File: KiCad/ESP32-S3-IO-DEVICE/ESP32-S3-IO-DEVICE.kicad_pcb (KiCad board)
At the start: 2 copper layers, 110 x 100 mm, 62 parts, among them J1 Terminal_04, J2 Terminal_04, J3 Terminal_06, J4 Terminal_02, J5 Terminal_04, J6 Terminal_06, Q1 2SC1815, Q10 2SC1815, Q11 2SC1815, Q12 2SC1815, Q2 2SC1815, Q3 2SC1815, Q4 2SC1815, Q5 2SC1815, Q6 2SC1815, Q7 2SC1815, Q8 2SC1815, Q9 2SC1815, U1 ESP32-S3-DevKitC

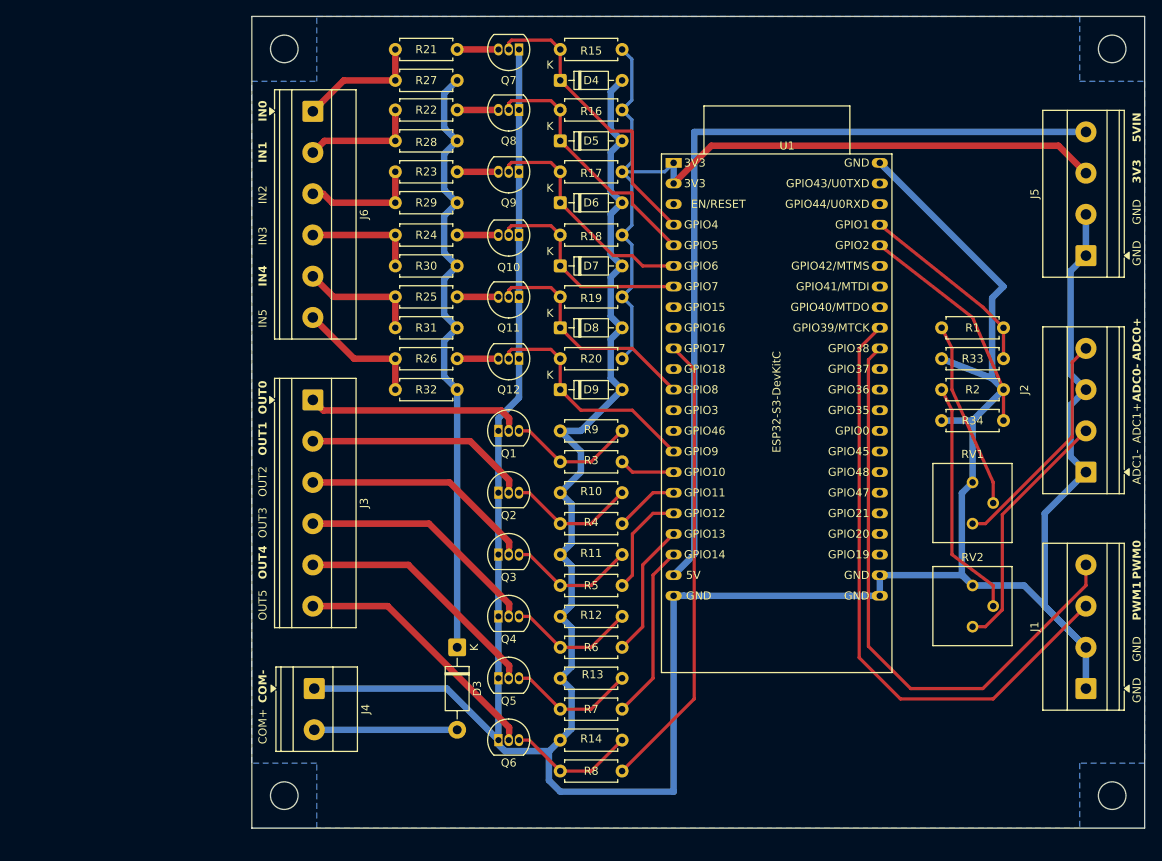
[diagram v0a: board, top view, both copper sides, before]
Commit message: Prepare ESP32IO for public release
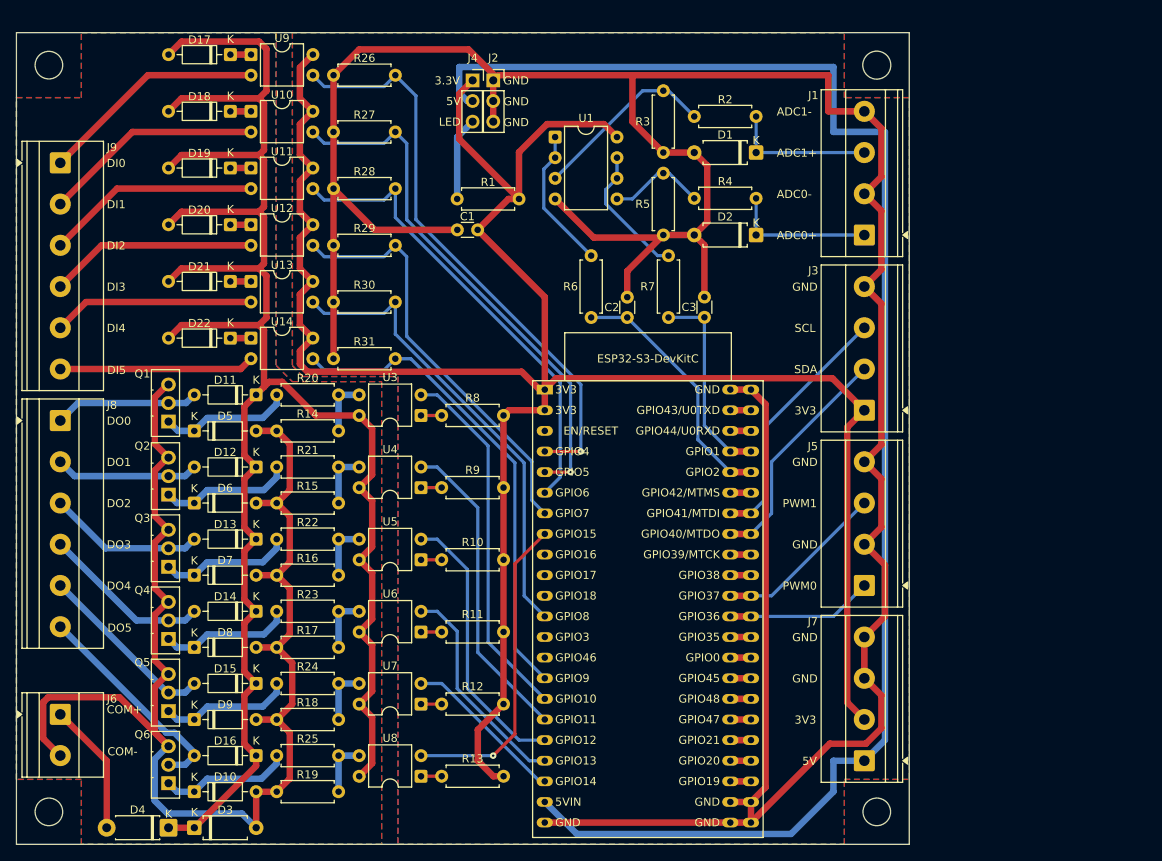
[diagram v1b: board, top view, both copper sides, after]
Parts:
- removed Q10, Q11, Q12, Q7, Q8, Q9: 2SC1815, Package_TO_SOT_THT:TO-92_Inline
- removed R32, R33: 10kΩ, Resistor_THT:R_Axial_DIN0207_L6.3mm_D2.5mm_P7.62mm_Horizontal
- removed R34: 15kΩ, Resistor_THT:R_Axial_DIN0207_L6.3mm_D2.5mm_P7.62mm_Horizontal
- removed RV1, RV2: 10kΩ, Potentiometer_THT:Potentiometer_Bourns_3386P_Vertical
- added C1: 0.1μF, Capacitor_THT:C_Disc_D3.0mm_W1.6mm_P2.50mm, F.Cu at (116.8, 74.3)
- added C2: 0.01μF, Capacitor_THT:C_Disc_D3.0mm_W1.6mm_P2.50mm, F.Cu at (135.3, 85.1)
- added C3: 0.01μF, Capacitor_THT:C_Disc_D3.0mm_W1.6mm_P2.50mm, F.Cu at (144.8, 85.1)
- added D1: P4KE15A, Diode_THT:D_A-405_P7.62mm_Horizontal, F.Cu at (151.1, 64.8)
- added D10: BZX55C12V, Diode_THT:D_DO-35_SOD27_P7.62mm_Horizontal, F.Cu at (81.9, 143.5)
- added D11: 1N4148, Diode_THT:D_DO-35_SOD27_P7.62mm_Horizontal, F.Cu at (89.5, 94.6)
- added D12: 1N4148, Diode_THT:D_DO-35_SOD27_P7.62mm_Horizontal, F.Cu at (89.5, 103.5)
- added D13: 1N4148, Diode_THT:D_DO-35_SOD27_P7.62mm_Horizontal, F.Cu at (89.5, 112.4)
- added D14: 1N4148, Diode_THT:D_DO-35_SOD27_P7.62mm_Horizontal, F.Cu at (89.5, 121.3)
- added D15: 1N4148, Diode_THT:D_DO-35_SOD27_P7.62mm_Horizontal, F.Cu at (89.5, 130.2)
- added D16: 1N4148, Diode_THT:D_DO-35_SOD27_P7.62mm_Horizontal, F.Cu at (89.5, 139.1)
- added D17: E-202, Diode_THT:D_DO-35_SOD27_P7.62mm_Horizontal, F.Cu at (86.4, 52.7)
- added D18: E-202, Diode_THT:D_DO-35_SOD27_P7.62mm_Horizontal, F.Cu at (86.4, 59.7)
- added D19: E-202, Diode_THT:D_DO-35_SOD27_P7.62mm_Horizontal, F.Cu at (86.4, 66.7)
- added D2: P4KE15A, Diode_THT:D_A-405_P7.62mm_Horizontal, F.Cu at (151.1, 74.9)
- added D20: E-202, Diode_THT:D_DO-35_SOD27_P7.62mm_Horizontal, F.Cu at (86.4, 73.7)
- added D21: E-202, Diode_THT:D_DO-35_SOD27_P7.62mm_Horizontal, F.Cu at (86.4, 80.7)
- added D22: E-202, Diode_THT:D_DO-35_SOD27_P7.62mm_Horizontal, F.Cu at (86.4, 87.6)
- added J7: Terminal_04, TerminalBlock_Phoenix:TerminalBlock_Phoenix_MKDS-1,5-4-5.08_1x04_P5.08mm_Horizontal, F.Cu at (164.5, 139.7)
- added J8: Terminal_06, TerminalBlock_Phoenix:TerminalBlock_Phoenix_MKDS-1,5-6-5.08_1x06_P5.08mm_Horizontal, F.Cu at (65.4, 97.8)
- added J9: Terminal_06, TerminalBlock_Phoenix:TerminalBlock_Phoenix_MKDS-1,5-6-5.08_1x06_P5.08mm_Horizontal, F.Cu at (65.4, 66.0)
- added U10: PC817, Package_DIP:DIP-4_W7.62mm, F.Cu at (88.9, 59.7)
- added U11: PC817, Package_DIP:DIP-4_W7.62mm, F.Cu at (88.9, 66.7)
- added U12: PC817, Package_DIP:DIP-4_W7.62mm, F.Cu at (88.9, 73.7)
- added U13: PC817, Package_DIP:DIP-4_W7.62mm, F.Cu at (88.9, 80.7)
- added U14: PC817, Package_DIP:DIP-4_W7.62mm, F.Cu at (88.9, 87.6)
- added U2: ESP32-S3-DevKitC, Espressif:ESP32-S3-DevKitC_3rd_party, F.Cu at (136.5, 119.4)
- added U3: PC817, Package_DIP:DIP-4_W7.62mm, F.Cu at (109.8, 97.2)
- added U4: PC817, Package_DIP:DIP-4_W7.62mm, F.Cu at (109.8, 106.1)
- added U5: PC817, Package_DIP:DIP-4_W7.62mm, F.Cu at (109.8, 114.9)
- added U6: PC817, Package_DIP:DIP-4_W7.62mm, F.Cu at (109.8, 123.8)
- added U7: PC817, Package_DIP:DIP-4_W7.62mm, F.Cu at (109.8, 132.7)
- added U8: PC817, Package_DIP:DIP-4_W7.62mm, F.Cu at (109.8, 141.6)
- added U9: PC817, Package_DIP:DIP-4_W7.62mm, F.Cu at (88.9, 52.7)
- D3: value 1N5819 -> P6KE33A; footprint Diode_THT:D_DO-41_SOD81_P10.16mm_Horizontal -> Diode_THT:D_A-405_P7.62mm_Horizontal
- D4: value BZX55C3V6 -> 1N5819; footprint Diode_THT:D_DO-35_SOD27_P7.62mm_Horizontal -> Diode_THT:D_DO-41_SOD81_P7.62mm_Horizontal
- D5, D6, D7, D8, D9: value BZX55C3V6 -> BZX55C12V
- J2: value Terminal_04 -> Socket_01x03; footprint TerminalBlock_Phoenix:TerminalBlock_Phoenix_MKDS-1,5-4-5.08_1x04_P5.08mm_Horizontal -> Connector_PinSocket_2.54mm:PinSocket_1x03_P2.54mm_Vertical
- J3: value Terminal_06 -> Terminal_04; footprint TerminalBlock_Phoenix:TerminalBlock_Phoenix_MKDS-1,5-6-5.08_1x06_P5.08mm_Horizontal -> TerminalBlock_Phoenix:TerminalBlock_Phoenix_MKDS-1,5-4-5.08_1x04_P5.08mm_Horizontal
- J4: value Terminal_02 -> Socket_01x03; footprint TerminalBlock_Phoenix:TerminalBlock_Phoenix_MKDS-1,5-2-5.08_1x02_P5.08mm_Horizontal -> Connector_PinSocket_2.54mm:PinSocket_1x03_P2.54mm_Vertical
- J6: value Terminal_06 -> Terminal_02; footprint TerminalBlock_Phoenix:TerminalBlock_Phoenix_MKDS-1,5-6-5.08_1x06_P5.08mm_Horizontal -> TerminalBlock_Phoenix:TerminalBlock_Phoenix_MKDS-1,5-2-5.08_1x02_P5.08mm_Horizontal
- Q1, Q2, Q3, Q4, Q5, Q6: value 2SC1815 -> 2SK4017; footprint Package_TO_SOT_THT:TO-92_Inline -> Package_TO_SOT_THT:TO-126-3_Vertical
- R1: value 15kΩ -> 2.2kΩ
- R10, R11, R12, R13, R9: value 100kΩ -> 330Ω
- R14: value 100kΩ -> 10kΩ
- R2: value 10kΩ -> 22kΩ
- R20: value 10kΩ -> 100Ω
- R21, R22, R23, R24, R25: value 47kΩ -> 100Ω
- R27, R28, R29, R30, R31: value 10kΩ -> 47kΩ
- R3, R5: value 680Ω -> 10kΩ
- R4: value 680Ω -> 22kΩ
- R6, R7: value 680Ω -> 100Ω
- R8: value 680Ω -> 330Ω
- U1: value ESP32-S3-DevKitC -> NJU7043D; footprint Espressif:ESP32-S3-DevKitC-1 -> Package_DIP:DIP-8_W7.62mm
- moved D4 104.0 mm to (78.7, 148.0), turned to 180 degrees
- moved J2 87.5 mm to (118.7, 55.9), turned to 0 degrees
- moved J6 80.5 mm to (65.4, 134.0)
- moved J4 77.4 mm to (116.2, 55.9), turned to 0 degrees
- moved R19 70.3 mm to (99.7, 143.5)
- moved R18 69.2 mm to (99.7, 134.6)
- moved R17 68.2 mm to (99.7, 125.7)
- moved J3 68.0 mm to (164.5, 96.5), turned to 90 degrees
- moved R16 67.1 mm to (99.7, 116.8)
- moved R15 65.9 mm to (99.7, 108.0)
- moved J1 62.2 mm to (164.5, 74.9)
- moved R1 61.8 mm to (114.3, 70.5)
- moved D9 60.7 mm to (81.9, 134.6)
- moved D8 59.9 mm to (81.9, 125.7)
- moved D7 59.0 mm to (81.9, 116.8)
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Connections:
- D3 pad 2: Net-(D3-A) -> COM-
- D4 pad 1: Net-(D4-K) -> COM+
- D4 pad 2: GND -> Net-(D4-A)
- D5 pad 2: GND -> COM-
- D6 pad 2: GND -> COM-
- D7 pad 2: GND -> COM-
- D8 pad 2: GND -> COM-
- D9 pad 2: GND -> COM-
- J1 pad 1: GND -> Net-(D2-K)
- J1 pad 3: Net-(J1-Pin_3) -> Net-(D1-K)
- J1 pad 4: Net-(J1-Pin_4) -> GND
- J2 pad 2: Net-(J2-Pin_2) -> GND
- J3 pad 1: Net-(J3-Pin_1) -> 3V3
- J3 pad 4: Net-(J3-Pin_4) -> GND
- J4 pad 1: GND -> 3V3
- J4 pad 2: Net-(D3-A) -> 5V
- J5 pad 1: GND -> Net-(J5-Pin_1)
- J5 pad 3: 3V3 -> Net-(J5-Pin_3)
- J5 pad 4: 5V -> GND
- J6 pad 1: Net-(J6-Pin_1) -> Net-(D4-A)
- J6 pad 2: Net-(J6-Pin_2) -> COM-
- Q1 pad 1: GND -> Net-(D5-K)
- Q1 pad 2: Net-(J3-Pin_1) -> Net-(D11-A)
- Q1 pad 3: Net-(Q1-B) -> COM-
- Q2 pad 1: GND -> Net-(D6-K)
- Q2 pad 2: Net-(J3-Pin_2) -> Net-(D12-A)
- Q2 pad 3: Net-(Q2-B) -> COM-
- Q3 pad 1: GND -> Net-(D7-K)
- Q3 pad 2: Net-(J3-Pin_3) -> Net-(D13-A)
- Q3 pad 3: Net-(Q3-B) -> COM-
- Q4 pad 1: GND -> Net-(D8-K)
- Q4 pad 2: Net-(J3-Pin_4) -> Net-(D14-A)
- Q4 pad 3: Net-(Q4-B) -> COM-
- Q5 pad 1: GND -> Net-(D9-K)
- Q5 pad 2: Net-(J3-Pin_5) -> Net-(D15-A)
- Q5 pad 3: Net-(Q5-B) -> COM-
- Q6 pad 1: GND -> Net-(D10-K)
- Q6 pad 2: Net-(J3-Pin_6) -> Net-(D16-A)
- Q6 pad 3: Net-(Q6-B) -> COM-
- R1 pad 1: Net-(R1-Pad1) -> Net-(J4-Pin_3)
- R1 pad 2: Net-(U1-GPIO1/ADC1_CH0) -> 3V3
- R10 pad 1: Net-(Q2-B) -> 3V3
- R10 pad 2: GND -> Net-(R10-Pad2)
- R11 pad 1: Net-(Q3-B) -> 3V3
- R11 pad 2: GND -> Net-(R11-Pad2)
- R12 pad 1: Net-(Q4-B) -> 3V3
- R12 pad 2: GND -> Net-(R12-Pad2)
- R13 pad 1: Net-(Q5-B) -> 3V3
- R13 pad 2: GND -> Net-(R13-Pad2)
- R14 pad 1: Net-(Q6-B) -> Net-(R14-Pad1)
- R14 pad 2: GND -> COM-
- R15 pad 1: 3V3 -> Net-(R15-Pad1)
- R15 pad 2: Net-(D4-K) -> COM-
- R16 pad 1: 3V3 -> Net-(R16-Pad1)
- R16 pad 2: Net-(D5-K) -> COM-
- R17 pad 1: 3V3 -> Net-(R17-Pad1)
- R17 pad 2: Net-(D6-K) -> COM-
- R18 pad 1: 3V3 -> Net-(R18-Pad1)
- R18 pad 2: Net-(D7-K) -> COM-
- R19 pad 1: 3V3 -> Net-(R19-Pad1)
- R19 pad 2: Net-(D8-K) -> COM-
- R2 pad 1: Net-(R2-Pad1) -> Net-(D1-K)
- R2 pad 2: Net-(U1-GPIO2/ADC1_CH1) -> Net-(U1A-+)
- R20 pad 1: 3V3 -> Net-(R14-Pad1)
- R20 pad 2: Net-(D9-K) -> Net-(D5-K)
- R21 pad 1: Net-(Q7-B) -> Net-(R15-Pad1)
- R21 pad 2: Net-(J6-Pin_1) -> Net-(D6-K)
- R22 pad 1: Net-(Q8-B) -> Net-(R16-Pad1)
- R22 pad 2: Net-(J6-Pin_2) -> Net-(D7-K)
- R23 pad 1: Net-(Q9-B) -> Net-(R17-Pad1)
- R23 pad 2: Net-(J6-Pin_3) -> Net-(D8-K)
- R24 pad 1: Net-(Q10-B) -> Net-(R18-Pad1)
- R24 pad 2: Net-(J6-Pin_4) -> Net-(D9-K)
- R25 pad 1: Net-(Q11-B) -> Net-(R19-Pad1)
- R25 pad 2: Net-(J6-Pin_5) -> Net-(D10-K)
- R26 pad 2: Net-(J6-Pin_6) -> GND
- R27 pad 1: COM+ -> Net-(U2-GPIO5/ADC1_CH4)
- R27 pad 2: Net-(J6-Pin_1) -> GND
- R28 pad 1: COM+ -> Net-(U2-GPIO6/ADC1_CH5)
- R28 pad 2: Net-(J6-Pin_2) -> GND
- R29 pad 1: COM+ -> Net-(U2-GPIO7/ADC1_CH6)
- R29 pad 2: Net-(J6-Pin_3) -> GND
- R3 pad 1: Net-(U1-GPIO10/ADC1_CH9) -> Net-(U1A-+)
- R3 pad 2: Net-(Q1-B) -> GND
- R30 pad 1: COM+ -> Net-(U2-GPIO8/ADC1_CH7)
- R30 pad 2: Net-(J6-Pin_4) -> GND
- R31 pad 1: COM+ -> Net-(U2-GPIO9/ADC1_CH8)
- R31 pad 2: Net-(J6-Pin_5) -> GND
- R4 pad 1: Net-(U1-GPIO11/ADC2_CH0) -> Net-(D2-K)
- R4 pad 2: Net-(Q2-B) -> Net-(U1B-+)
- R5 pad 1: Net-(U1-GPIO12/ADC2_CH1) -> Net-(U1B-+)
- R5 pad 2: Net-(Q3-B) -> GND
- R6 pad 1: Net-(U1-GPIO13/ADC2_CH2) -> Net-(U1A--)
- R6 pad 2: Net-(Q4-B) -> Net-(U2-GPIO2/ADC1_CH1)
- R7 pad 1: Net-(U1-GPIO14/ADC2_CH3) -> Net-(U1B--)
- R7 pad 2: Net-(Q5-B) -> Net-(U2-GPIO1/ADC1_CH0)
- R8 pad 1: Net-(U1-GPIO17/ADC2_CH6) -> 3V3
- R8 pad 2: Net-(Q6-B) -> Net-(R8-Pad2)
- R9 pad 1: Net-(Q1-B) -> 3V3
- R9 pad 2: GND -> Net-(R9-Pad2)
- U1 pad 1: 3V3 -> Net-(U1A--)
- U1 pad 2: 3V3 -> Net-(U1A--)
- U1 pad 3: unconnected-(U1-CHIP_PU-Pad3) -> Net-(U1A-+)
- U1 pad 4: Net-(D4-K) -> GND
- U1 pad 5: Net-(D5-K) -> Net-(U1B-+)
- U1 pad 6: Net-(D6-K) -> Net-(U1B--)
- U1 pad 7: Net-(D7-K) -> Net-(U1B--)
- U1 pad 8: unconnected-(U1-GPIO15/ADC2_CH4/32K_P-Pad8) -> 3V3
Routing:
- net 3V3: track 106.5 -> 282.1 mm
- net COM+: track 76.5 -> 248.6 mm
- net COM-: track 0.00 -> 169.9 mm
- net 5V: track 103.9 -> 191.2 mm
- net Net-(J1-Pin_3): track 76.5 -> 0.00 mm
- net Net-(J1-Pin_4): track 74.0 -> 0.00 mm
- net Net-(U2-GPIO4/ADC1_CH3): track 5.03 -> 71.6 mm, vias 0 -> 1
- net Net-(U2-GPIO5/ADC1_CH4): track 0.00 -> 65.3 mm, vias 0 -> 1
- net GND: track 447.7 -> 386.9 mm
- net Net-(U2-GPIO9/ADC1_CH8): track 0.00 -> 59.4 mm
- net Net-(U2-GPIO6/ADC1_CH5): track 0.00 -> 58.0 mm
- net Net-(U2-GPIO8/ADC1_CH7): track 0.00 -> 57.7 mm
- net Net-(U1-GPIO17/ADC2_CH6): track 56.8 -> 0.00 mm
- net Net-(U2-GPIO7/ADC1_CH6): track 0.00 -> 52.0 mm
- net Net-(U2-GPIO10/ADC1_CH9): track 0.00 -> 44.9 mm
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- added copper zone on B.Cu, net COM-
- added copper zone on F.Cu, net COM-
- added copper zone on F.Cu, net GND
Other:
- board text added: "3.3V"
- board text added: "5V"
- board text added: "DI0"
- board text added: "DI1"
- board text added: "DI2"
- board text added: "DI3"
- board text added: "DI4"
- board text added: "DI5"
- board text added: "DO0"
- board text added: "DO1"
- board text added: "DO2"
- board text added: "DO3"
- board text added: "DO4"
- board text added: "DO5"
- board text added: "LED"
- board text added: "SCL"
- board text added: "SDA"
- board text removed: "5VIN"
- board text removed: "IN0"
- board text removed: "IN1"
- board text removed: "IN2"
- board text removed: "IN3"
- board text removed: "IN4"
- board text removed: "IN5"
- board text removed: "OUT0"
- board text removed: "OUT1"
- board text removed: "OUT2"
- board text removed: "OUT3"
- board text removed: "OUT4"
- board text removed: "OUT5"
